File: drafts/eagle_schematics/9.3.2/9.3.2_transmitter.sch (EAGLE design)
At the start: 15 parts, among them Q1 BC847BS, Q2A BC857BS, Q3 2N7002, Q4B BC857BS

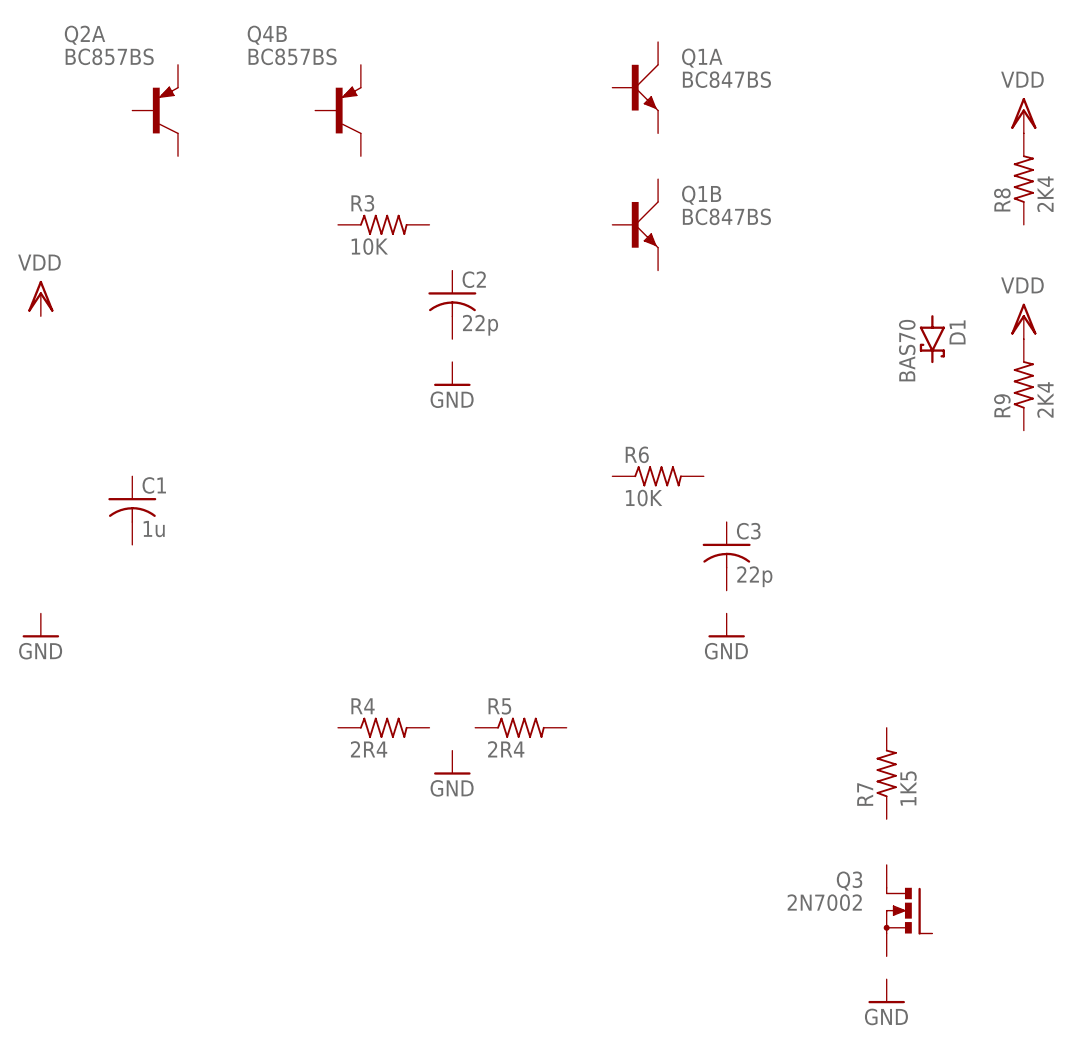
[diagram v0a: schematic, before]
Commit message: Update RailCom reference circuits.
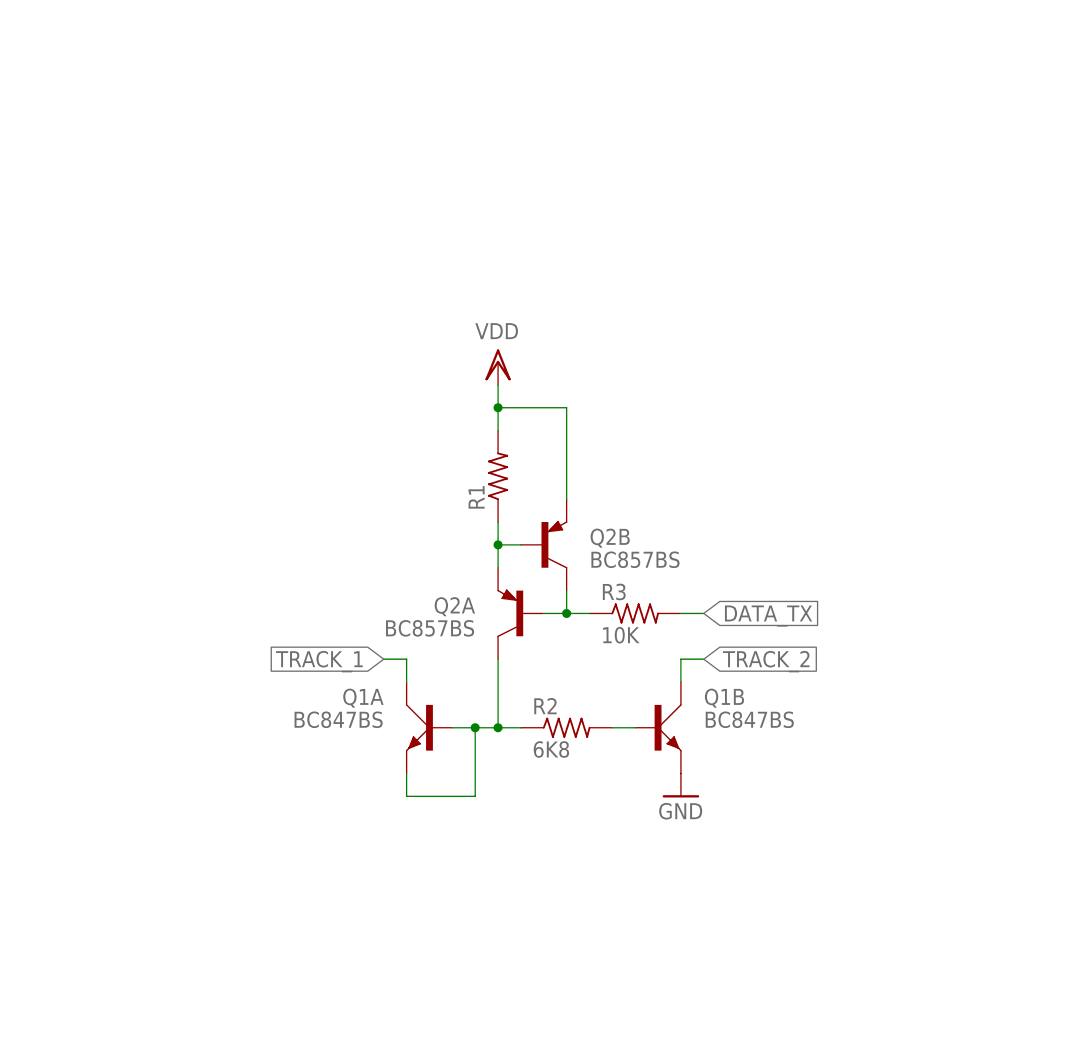
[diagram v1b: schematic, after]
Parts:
- removed C1: 1u, rcl:C-USC0402
- removed C2, C3: 22p, rcl:C-USC0402
- removed D1: BAS70, diode:BAS70
- removed Q3: 2N7002, transistor-power:IRF512
- removed Q4B: BC857BS, transistor-pnp:BC857BSMD
- removed R4, R5: 2R4, resistor:R-US_R1206
- removed R6: 10K, resistor:R-US_R0402
- removed R7: 1K5, resistor:R-US_R1206
- removed R8, R9: 2K4, resistor:R-US_R0402
- added Q2B: BC857BS, transistor-pnp:BC857BSMD
- added R1: 22R, resistor:R-US_R0402
- added R2: 6K8, resistor:R-US_R0402
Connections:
- new net DATA_TX: R3.2
- new net GND: Q1B.E
- new net N$1: Q2A.E, Q2B.B, R1.1
- new net N$2: Q2A.B, Q2B.C, R3.1
- new net N$3: Q1B.B, R2.2
- new net N$4: Q1A.B, Q1A.E, Q2A.C, R2.1
- new net TRACK_1: Q1A.C
- new net TRACK_2: Q1B.C
- net VDD: now also Q2B.E, R1.2; no longer R8.2, R9.2
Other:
- moved on the sheet: Q1A, Q1B, Q2A, R3
